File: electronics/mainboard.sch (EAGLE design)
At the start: 84 parts, among them T1 NPN_BC817,215, T2 NPN_BC817,215, T3 NPN_BC817,215, U1 CD4051BM, X1 JST-XH-10-PIN-LONG-PAD, X2 JST-XH-10-PIN-LONG-PAD, X3 JST-XH-10-PIN-LONG-PAD, X4 JST-XH-10-PIN-LONG-PAD, X5 JST-XH-10-PIN-LONG-PAD

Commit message: Board tweaks
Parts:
- added CA1, CA2, CA3, CA4, CA5, CA6, CA7: C_EU-100NF, rhoban:C_EU-100NF
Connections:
- net 3.3: now also CA1.1, CA3.1
- net GND: now also CA1.2, CA2.2, CA3.2, CA4.2, CA5.2, CA6.2, CA7.2
- net VCC: now also CA2.1, CA4.1, CA5.1, CA6.1, CA7.1
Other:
- moved on the sheet: C1, C17, C18, C2, C3, C4, C5, C6, ENC1, ENC2, ENC3, ENC4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

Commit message: 2nd xt60 connector
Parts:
- added XT1: CONNEC_ALIM, rhoban:CONNEC_ALIM
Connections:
- net GND: now also XT1.GND
- net VIN: now also XT1.V+
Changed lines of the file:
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@@
 <class number="0" name="default" width="0.254" drill="0">
-</class>
-<class number="1" name="alime" width="0.254" drill="0">
 </class>
 <class number="2" name="alim_big" width="1.524" drill="0">
@@
 <part name="GND9" library="supply1" deviceset="GND" device=""/>
 <part name="CA7" library="rhoban" deviceset="C_EU" device="-100NF"/>
+<part name="XT1" library="rhoban" deviceset="CONNEC_ALIM" device=""/>
 </parts>
 <sheets>
@@
 <plain>
 <text x="-63.5" y="20.32" size="7.62" layer="104">IMU</text>
-<text x="-160.02" y="114.3" size="6.4516" layer="95">POWER</text>
+<text x="-160.02" y="132.08" size="6.4516" layer="95">POWER</text>
 <text x="-55.88" y="111.76" size="6.4516" layer="95">MCU</text>
 <text x="-157.48" y="20.32" size="6.4516" layer="95">BUZZER</text>
@@
 <instance part="GND9" gate="1" x="104.14" y="-50.8"/>
 <instance part="CA7" gate="G$1" x="104.14" y="-43.18"/>
+<instance part="XT1" gate="G$1" x="-162.56" y="111.76"/>
 </instances>
 <busses>
@@
 <wire x1="104.14" y1="-48.26" x2="104.14" y2="-45.72" width="0.1524" layer="91"/>
 </segment>
+<segment>
+<pinref part="XT1" gate="G$1" pin="GND"/>
+<wire x1="-167.64" y1="116.84" x2="-175.26" y2="116.84" width="0.1524" layer="91"/>
+<label x="-180.34" y="116.84" size="1.778" layer="95"/>
+</segment>
 </net>
 <net name="N$4" class="0">
@@
 <label x="35.56" y="-7.62" size="1.778" layer="95"/>
 </segment>
+<segment>
+<pinref part="XT1" gate="G$1" pin="V+"/>
+<wire x1="-167.64" y1="121.92" x2="-175.26" y2="121.92" width="0.1524" layer="91"/>
+<label x="-180.34" y="121.92" size="1.778" layer="95"/>
+</segment>
 </net>

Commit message: README
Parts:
- R5: value 60 -> 62
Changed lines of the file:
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@@
 <part name="T2" library="rhoban" deviceset="NPN" device="_BC817,215"/>
 <part name="R4" library="rhoban" deviceset="RESISTANCE" device="-R0805" value="1K"/>
-<part name="R5" library="rhoban" deviceset="RESISTANCE" device="-R0805" value="60"/>
+<part name="R5" library="rhoban" deviceset="RESISTANCE" device="-R0805" value="62"/>
 <part name="R6" library="rhoban" deviceset="RESISTANCE" device="-R0805" value="10K"/>
 <part name="ENC1" library="rhoban" deviceset="LS7366R" device="SO14"/>

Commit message: Updating board
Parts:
- R5: value 62 -> 110
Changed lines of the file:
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@@
 <part name="T2" library="rhoban" deviceset="NPN" device="_BC817,215"/>
 <part name="R4" library="rhoban" deviceset="RESISTANCE" device="-R0805" value="1K"/>
-<part name="R5" library="rhoban" deviceset="RESISTANCE" device="-R0805" value="62"/>
+<part name="R5" library="rhoban" deviceset="RESISTANCE" device="-R0805" value="110"/>
 <part name="R6" library="rhoban" deviceset="RESISTANCE" device="-R0805" value="10K"/>
 <part name="ENC1" library="rhoban" deviceset="LS7366R" device="SO14"/>

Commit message: Adding PWM compatibility pins
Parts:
- added PWM1, PWM2, PWM3, PWM4, PWM5: CONNEC_1X03, rhoban:CONNEC_1X03
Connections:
- net GND: now also PWM1.1, PWM2.1, PWM3.1, PWM4.1, PWM5.1
- net M1_SPEED: now also PWM1.3
- net M2_SPEED: now also PWM2.3
- net M3_SPEED: now also PWM3.3
- net M4_SPEED: now also PWM4.3
- net M5_SPEED: now also PWM5.3
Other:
- moved on the sheet: CA1, CA2, CA3, COM1, COM2, COM3, EMIT, MAPLE, POWERCAP1, POWERCAP2, R1, R10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

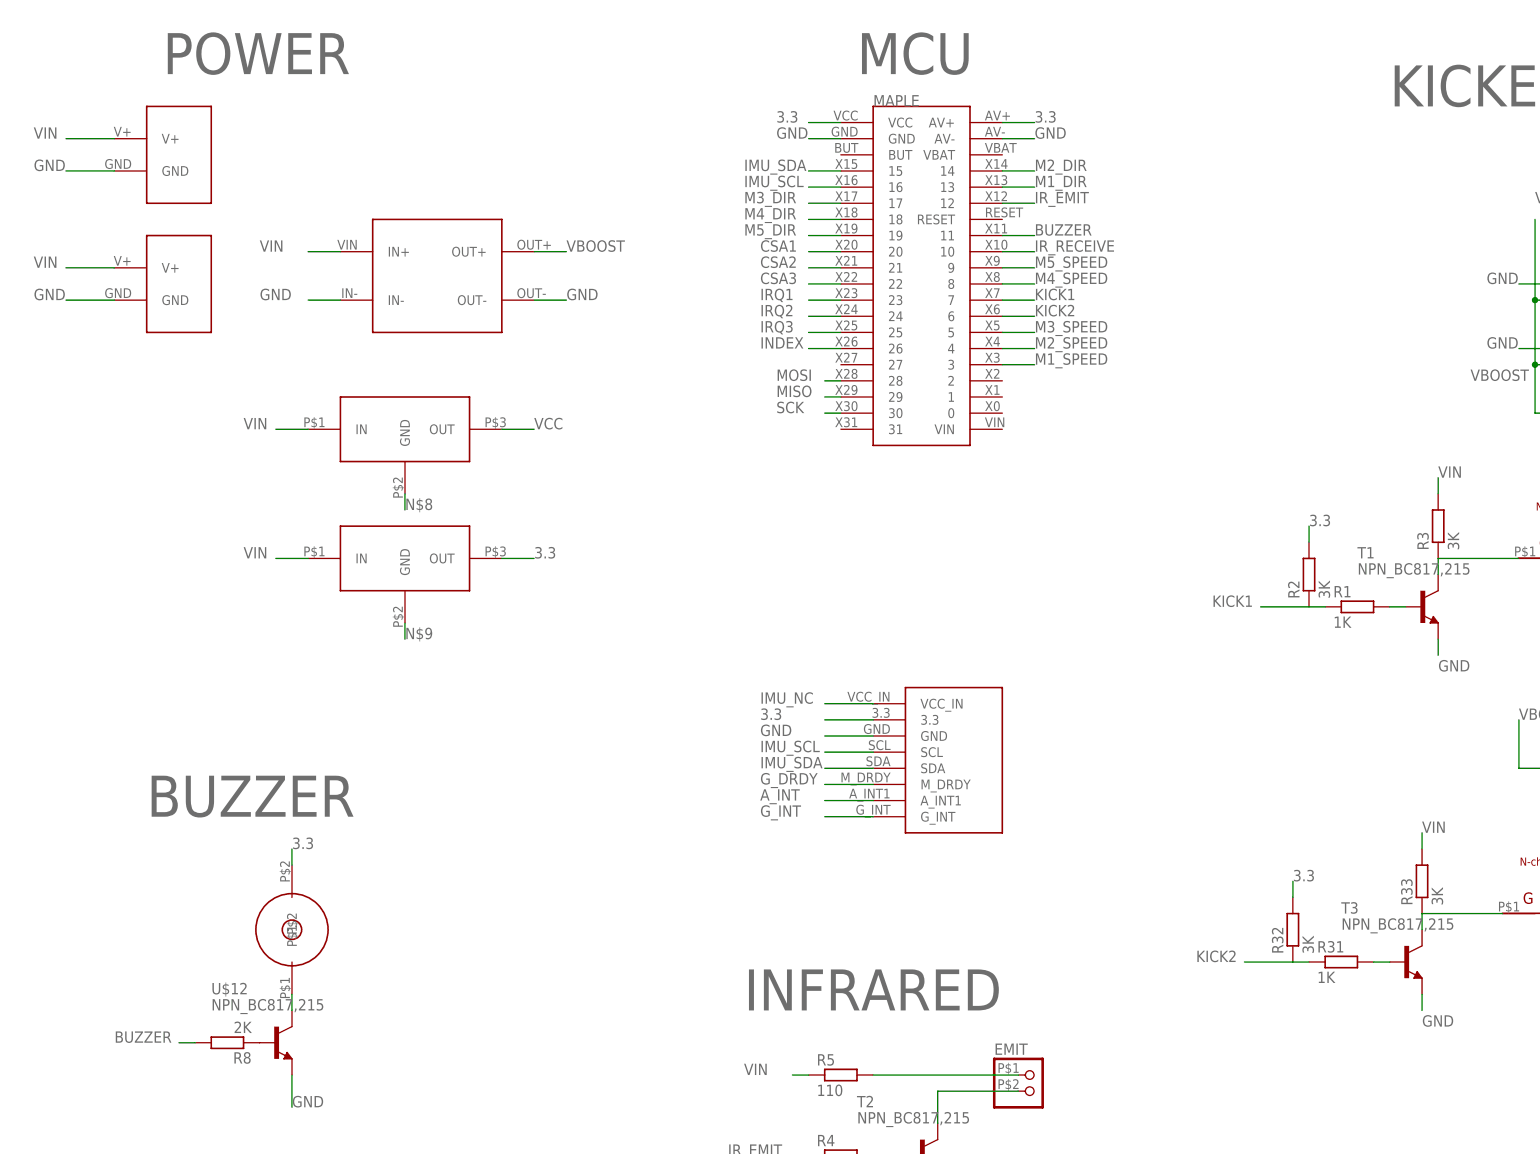
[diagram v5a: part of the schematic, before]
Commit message: Adding boost_en and cap to control charge
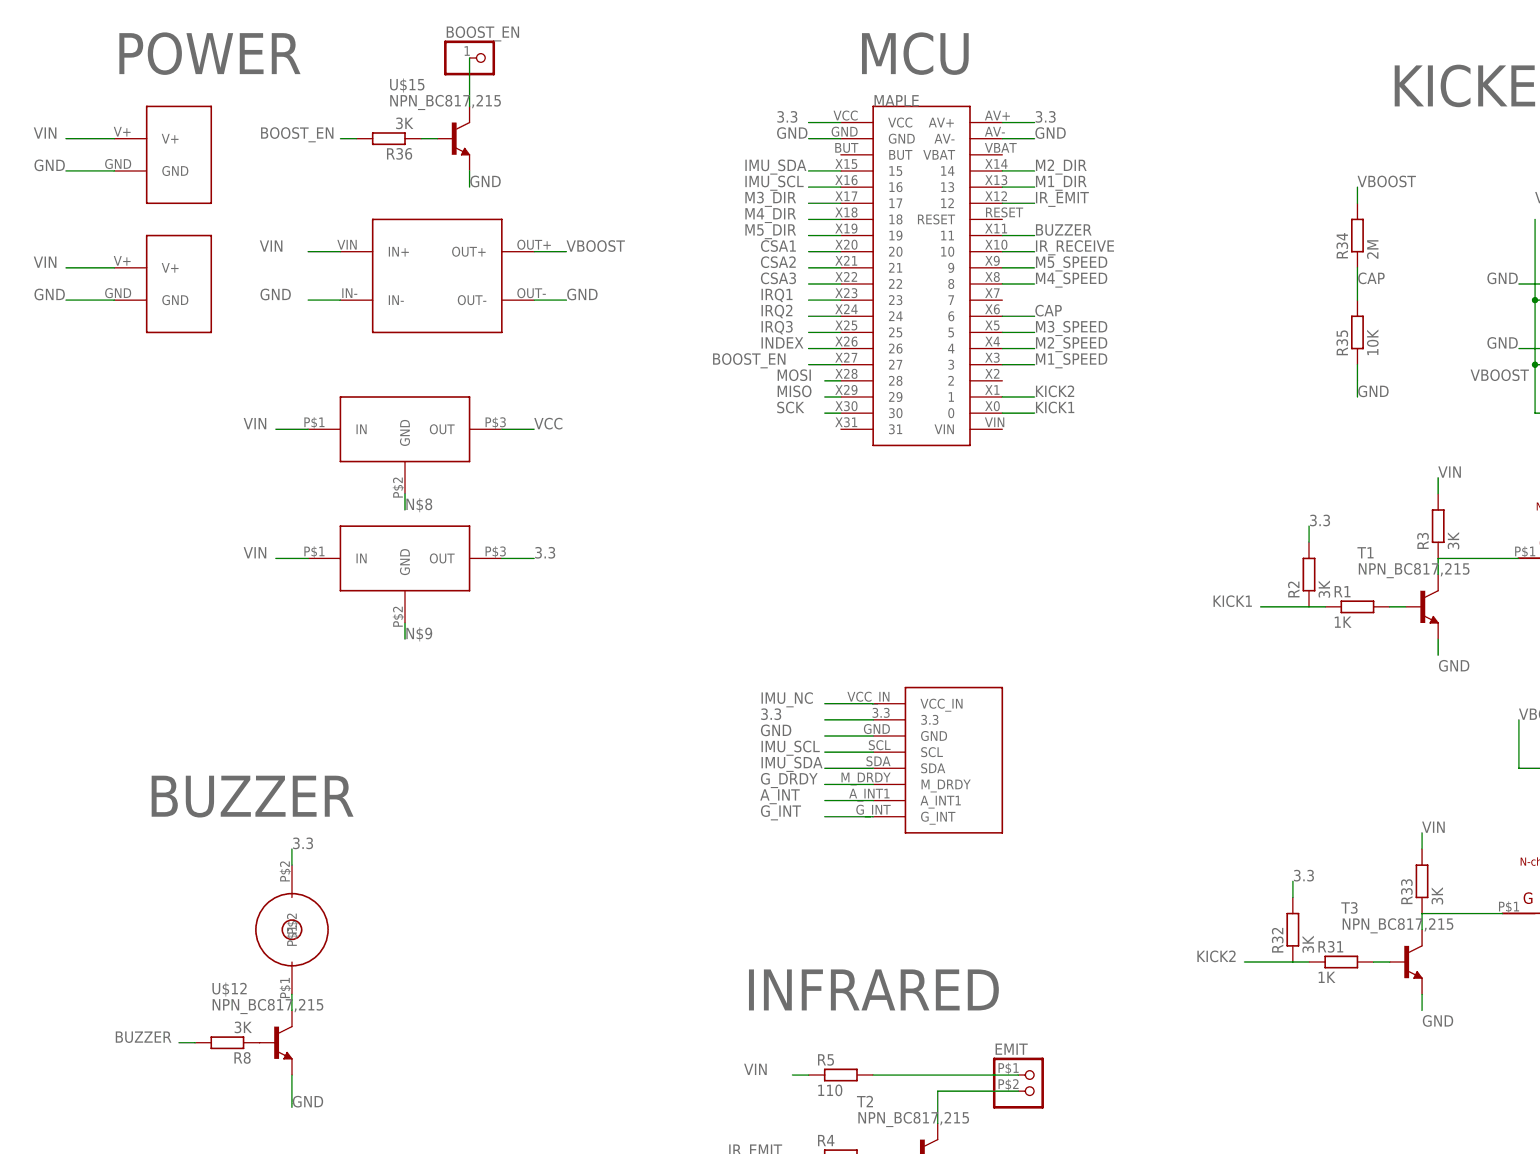
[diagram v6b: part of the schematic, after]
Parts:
- added BOOST_EN: CONNEC_1X01, rhoban:CONNEC_1X01
- added R34: 2M, rhoban:RESISTANCE-R0805
- added R35: 10K, rhoban:RESISTANCE-R0805
- added R36: 3K, rhoban:RESISTANCE-R0805
- added U$15: NPN_BC817,215, rhoban:NPN_BC817,215
- R8: value 2K -> 3K
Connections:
- new net BOOST_EN: MAPLE.27, R36.2
- new net CAP: MAPLE.6, R34.1, R35.2
- new net N$37: BOOST_EN.1, U$15.C
- new net N$38: R36.1, U$15.B
- net GND: now also R35.1, U$15.E
- net KICK1: now also MAPLE.0; no longer MAPLE.7
- net KICK2: now also MAPLE.1; no longer MAPLE.6
- net VBOOST: now also R34.2
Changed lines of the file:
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@@
 <part name="POWERCAP1" library="rhoban" deviceset="CONNEC_1X02" device="BIG"/>
 <part name="U$12" library="rhoban" deviceset="NPN" device="_BC817,215"/>
-<part name="R8" library="rcl" deviceset="R-EU_" device="R0805" value="2K"/>
+<part name="R8" library="rcl" deviceset="R-EU_" device="R0805" value="3K"/>
 <part name="U$13" library="rhoban" deviceset="BUZZER" device="66"/>
 <part name="U$2" library="rhoban" deviceset="GY-85" device=""/>
@@
 <part name="PWM4" library="rhoban" deviceset="CONNEC_1X03" device=""/>
 <part name="PWM5" library="rhoban" deviceset="CONNEC_1X03" device=""/>
+<part name="BOOST_EN" library="rhoban" deviceset="CONNEC_1X01" device=""/>
+<part name="R34" library="rhoban" deviceset="RESISTANCE" device="-R0805" value="2M"/>
+<part name="R35" library="rhoban" deviceset="RESISTANCE" device="-R0805" value="10K"/>
+<part name="U$15" library="rhoban" deviceset="NPN" device="_BC817,215"/>
+<part name="R36" library="rhoban" deviceset="RESISTANCE" device="-R0805" value="3K"/>
 </parts>
 <sheets>
@@
 <plain>
 <text x="-58.42" y="40.64" size="7.62" layer="104">IMU</text>
-<text x="-160.02" y="132.08" size="6.4516" layer="95">POWER</text>
+<text x="-167.64" y="132.08" size="6.4516" layer="95">POWER</text>
 <text x="-50.8" y="132.08" size="6.4516" layer="95">MCU</text>
 <text x="-162.56" y="15.24" size="6.4516" layer="95">BUZZER</text>
@@
 <instance part="PWM4" gate="G$1" x="381" y="-35.56"/>
 <instance part="PWM5" gate="G$1" x="312.42" y="-88.9"/>
+<instance part="BOOST_EN" gate="G$1" x="-114.3" y="134.62"/>
+<instance part="R34" gate="G$1" x="27.94" y="106.68" rot="R90"/>
+<instance part="R35" gate="G$1" x="27.94" y="91.44" rot="R90"/>
+<instance part="U$15" gate="G$1" x="-114.3" y="121.92"/>
+<instance part="R36" gate="G$1" x="-124.46" y="121.92" rot="R180"/>
 </instances>
 <busses>
@@
 <net name="KICK2" class="0">
 <segment>
-<pinref part="MAPLE" gate="G$1" pin="6"/>
-<wire x1="-27.94" y1="93.98" x2="-22.86" y2="93.98" width="0.1524" layer="91"/>
-<label x="-22.86" y="93.98" size="1.778" layer="95"/>
-</segment>
-<segment>
 <pinref part="R31" gate="G$1" pin="1"/>
 <pinref part="R32" gate="G$1" pin="1"/>
@@
 <wire x1="17.78" y1="-7.62" x2="10.16" y2="-7.62" width="0.1524" layer="91"/>
 <label x="2.54" y="-7.62" size="1.778" layer="95"/>
+</segment>
+<segment>
+<pinref part="MAPLE" gate="G$1" pin="1"/>
+<wire x1="-27.94" y1="81.28" x2="-22.86" y2="81.28" width="0.1524" layer="91"/>
+<label x="-22.86" y="81.28" size="1.778" layer="95"/>
 </segment>
 </net>
@@
 <wire x1="314.96" y1="-83.82" x2="307.34" y2="-83.82" width="0.1524" layer="91"/>
 <label x="302.26" y="-83.82" size="1.778" layer="95"/>
+</segment>
+<segment>
+<pinref part="R35" gate="G$1" pin="1"/>
+<wire x1="27.94" y1="86.36" x2="27.94" y2="83.82" width="0.1524" layer="91"/>
+<wire x1="27.94" y1="81.28" x2="27.94" y2="83.82" width="0.1524" layer="91"/>
+<label x="27.94" y="81.28" size="1.778" layer="95"/>
+</segment>
+<segment>
+<pinref part="U$15" gate="G$1" pin="E"/>
+<wire x1="-111.76" y1="116.84" x2="-111.76" y2="114.3" width="0.1524" layer="91"/>
+<label x="-111.76" y="114.3" size="1.778" layer="95"/>
 </segment>
 </net>
@@
 <label x="53.34" y="30.48" size="1.778" layer="95"/>
 </segment>
+<segment>
+<pinref part="R34" gate="G$1" pin="2"/>
+<wire x1="27.94" y1="111.76" x2="27.94" y2="114.3" width="0.1524" layer="91"/>
+<label x="27.94" y="114.3" size="1.778" layer="95"/>
+</segment>
 </net>
 <net name="BUZZER" class="0">
@@
 </segment>
 <segment>
-<pinref part="MAPLE" gate="G$1" pin="7"/>
-<wire x1="-27.94" y1="96.52" x2="-22.86" y2="96.52" width="0.1524" layer="91"/>
-<label x="-22.86" y="96.52" size="1.778" layer="95"/>
-</segment>
-</net>
+<pinref part="MAPLE" gate="G$1" pin="0"/>
+<wire x1="-27.94" y1="78.74" x2="-22.86" y2="78.74" width="0.1524" layer="91"/>
+<label x="-22.86" y="78.74" size="1.778" layer="95"/>
+</segment>
+</net>
+<net name="BOOST_EN" class="0">
+<segment>
+<pinref part="MAPLE" gate="G$1" pin="27"/>
+<wire x1="-53.34" y1="86.36" x2="-58.42" y2="86.36" width="0.1524" layer="91"/>
+<label x="-73.66" y="86.36" size="1.778" layer="95"/>
+</segment>
+<segment>
+<pinref part="R36" gate="G$1" pin="2"/>
+<wire x1="-129.54" y1="121.92" x2="-132.08" y2="121.92" width="0.1524" layer="91"/>
+<label x="-144.78" y="121.92" size="1.778" layer="95"/>
+</segment>
+</net>
+<net name="CAP" class="0">
+<segment>
+<pinref part="MAPLE" gate="G$1" pin="6"/>
+<wire x1="-27.94" y1="93.98" x2="-22.86" y2="93.98" width="0.1524" layer="91"/>
+<label x="-22.86" y="93.98" size="1.778" layer="95"/>
+</segment>
+<segment>
+<pinref part="R34" gate="G$1" pin="1"/>
+<pinref part="R35" gate="G$1" pin="2"/>
+<wire x1="27.94" y1="101.6" x2="27.94" y2="96.52" width="0.1524" layer="91"/>
+<label x="27.94" y="99.06" size="1.778" layer="95"/>
+</segment>
+</net>
+<net name="N$38" class="0">
+<segment>
+<pinref part="U$15" gate="G$1" pin="B"/>
+<pinref part="R36" gate="G$1" pin="1"/>
+<wire x1="-119.38" y1="121.92" x2="-116.84" y2="121.92" width="0.1524" layer="91"/>
+</segment>
+</net>
+<net name="N$37" class="0">
+<segment>
+<pinref part="U$15" gate="G$1" pin="C"/>
+<pinref part="BOOST_EN" gate="G$1" pin="1"/>
+<wire x1="-111.76" y1="127" x2="-111.76" y2="134.62" width="0.1524" layer="91"/>
+</segment>
+</net>
